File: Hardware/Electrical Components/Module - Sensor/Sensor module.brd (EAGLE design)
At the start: 40 x 70 mm, 29 parts

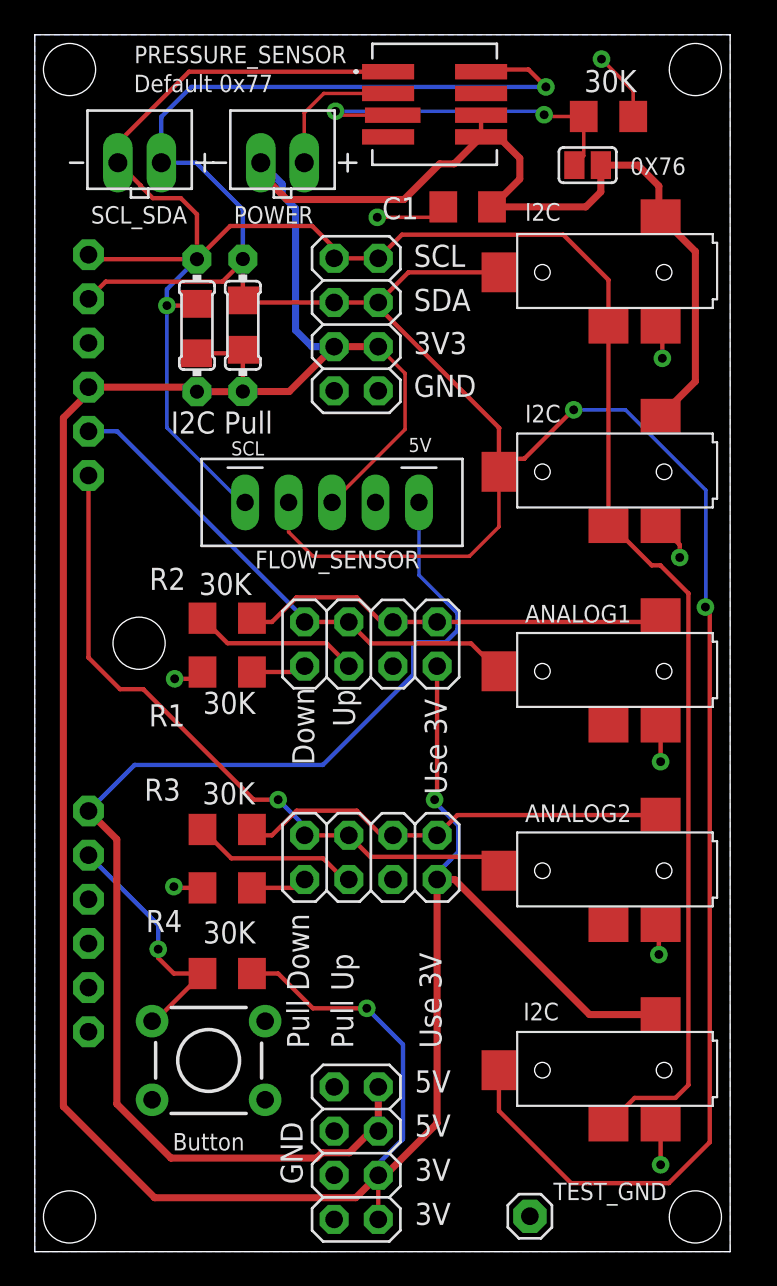
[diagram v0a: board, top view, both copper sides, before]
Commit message: Major fix for sensor module
O Power Module: Changes in footprint location of motor push-to-connect for mounting place. Move the 90-angle header further inside for better mechanical support
O Sensor Module: Rearrange 2.5mm headphone jack closer to the edge for proper mounting. The older version stops the male jack fully dock with the female casing thus fail to connect. Move the 90-angle header further inside for better mechanical support.
O MS5803-02BA: Change symbol, change SDA -> SDO. This label caused the PCB to stop working with all I2C devices. Sensor Module: Rewire to the write SDA, tested.
+ Add MS5803-02BA Datasheet
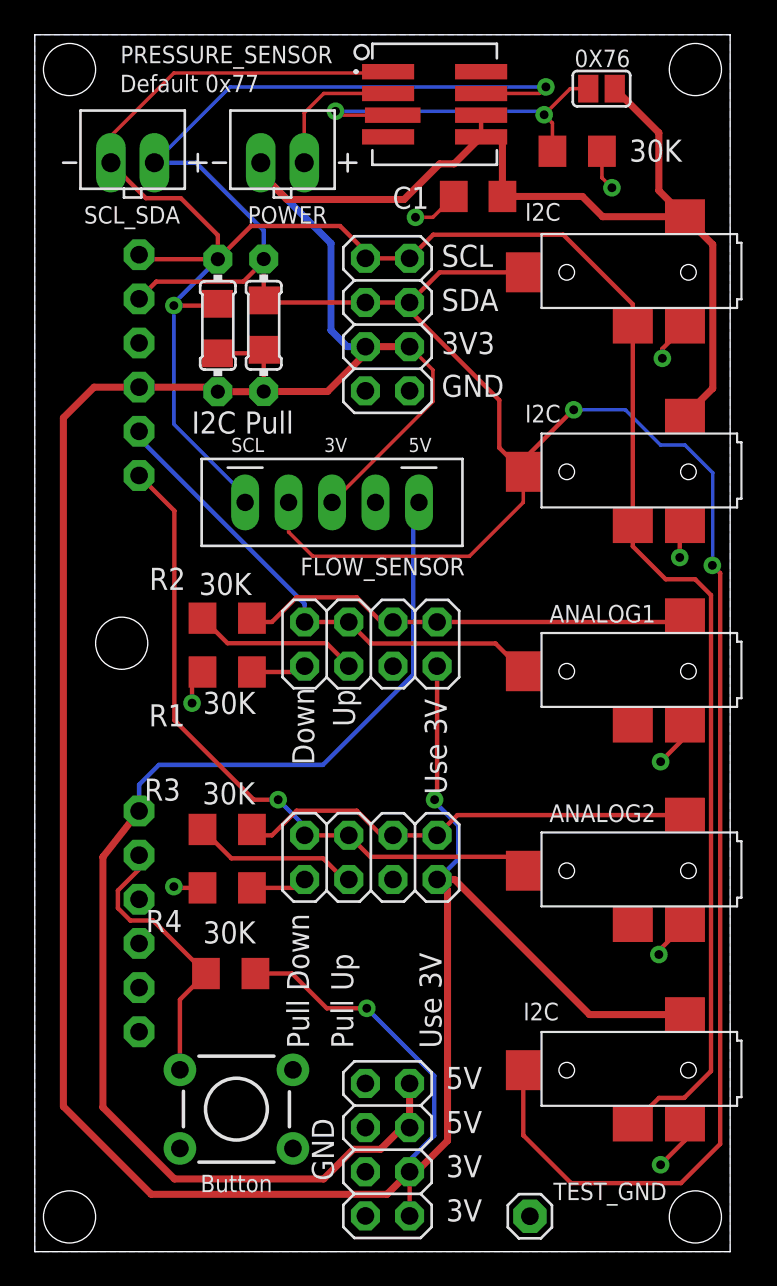
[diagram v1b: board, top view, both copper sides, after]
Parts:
- moved 0X76 4.47 mm to (32.6, 66.9)
- moved S1 3.22 mm to (11.6, 8.20)
- moved TO_LOGIC_BOARD1 2.91 mm to (6.00, 51.0)
- moved TO_LOGIC_BOARD2 2.91 mm to (6.00, 19.0)
- moved R10 2.69 mm to (31.2, 63.3)
- moved POWER_3-5 1.81 mm to (20.3, 5.87)
- moved I2C_1 1.80 mm to (20.3, 53.3)
- moved ANALOG1 1.40 mm to (37.4, 36.6)
- moved ANALOG2 1.40 mm to (37.4, 25.1)
- moved U$1 1.40 mm to (37.4, 59.5)
- moved U$2 1.40 mm to (37.4, 13.6)
- moved U$5 1.40 mm to (37.4, 48.1)
- moved R5 1.20 mm to (10.5, 53.1)
- moved R6 1.20 mm to (13.2, 53.3)
- moved R7 1.20 mm to (13.2, 53.3)
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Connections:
- removed net N$11: PRESSURE_SENSOR.7
- net SDA: now also PRESSURE_SENSOR.7; no longer PRESSURE_SENSOR.8
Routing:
- net +3V3: track 229.3 -> 239.5 mm
- net BUTTON1: track 14.5 -> 16.3 mm, vias 1 -> 0
- net SDA: track 167.1 -> 165.6 mm
- net N$7: track 25.3 -> 26.7 mm
- net N$3: track 24.9 -> 26.3 mm
- net SENSOR1: track 29.7 -> 28.7 mm
- net +5V: track 71.8 -> 70.8 mm
- net GND: track 30.1 -> 29.2 mm
- net SENSOR2: track 39.5 -> 38.9 mm
